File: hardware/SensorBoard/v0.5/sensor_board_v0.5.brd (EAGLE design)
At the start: 46.8 x 39.9 mm, 58 parts, among them J3 USB-MICROB, U1 ATMEGA328P, U2 TSL2561, U4 MPL115A, U5 FT231XS, U6 ADMP401, U7 SHT31-DIS, U8 MCP1703CB, U9 MCP1703CB, Y1 16MHZ

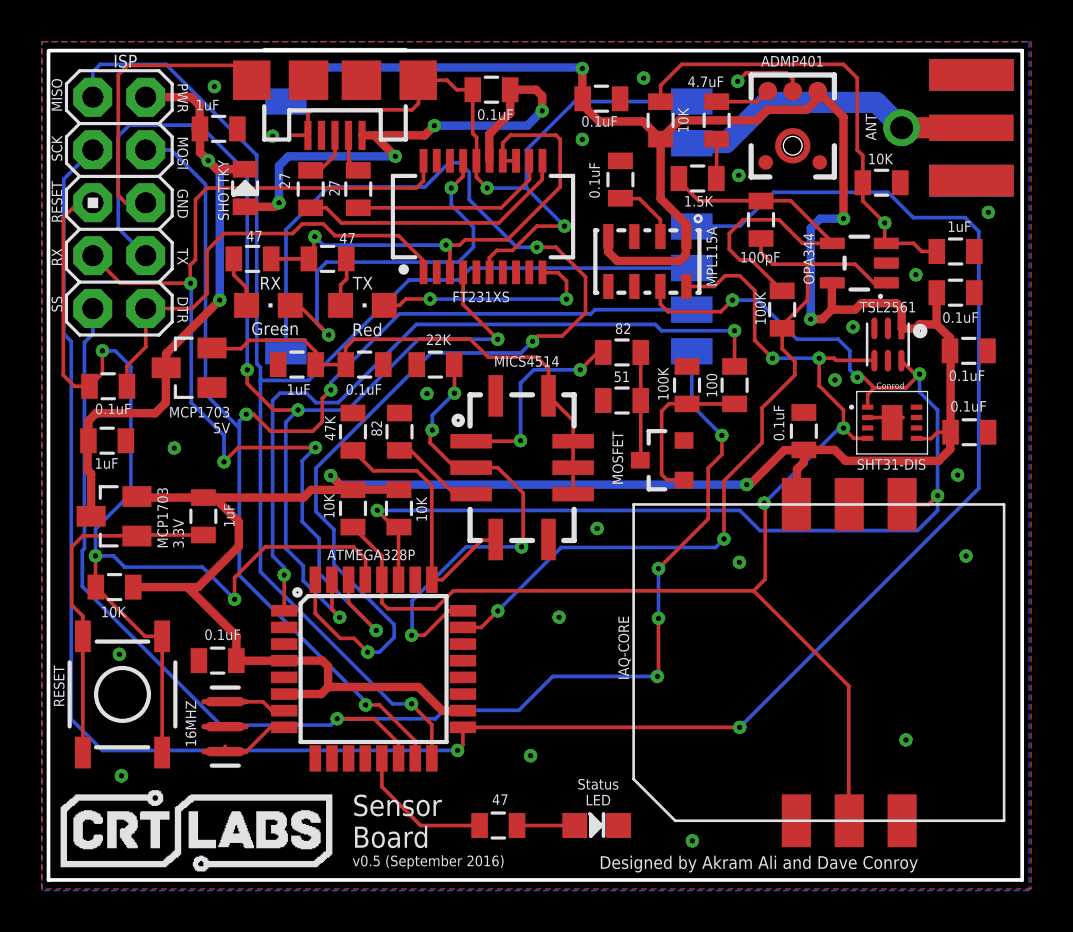
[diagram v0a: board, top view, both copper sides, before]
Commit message: Adjusted silk screen
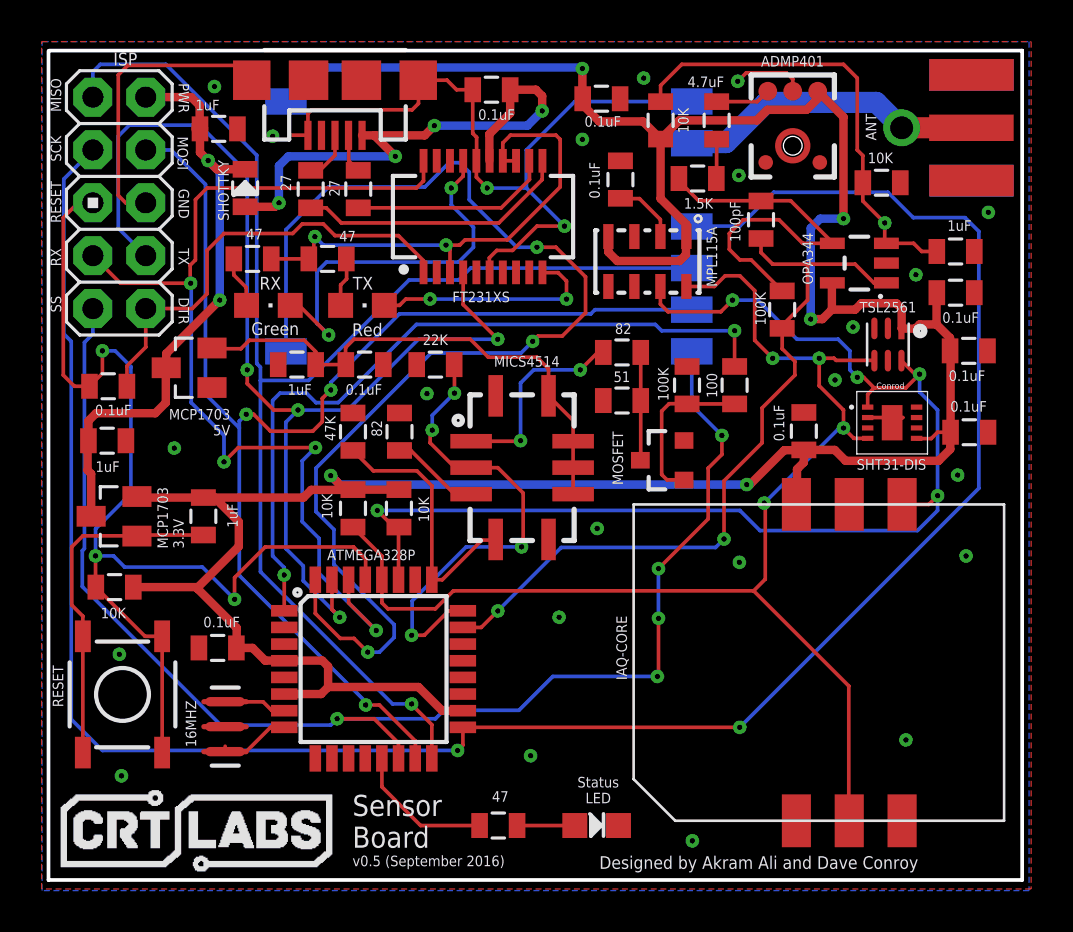
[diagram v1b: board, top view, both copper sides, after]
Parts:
- moved C15 0.61 mm to (14.0, 17.8)
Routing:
- net VCC: track 148.1 -> 147.6 mm

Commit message: Made the GND plane more consistent
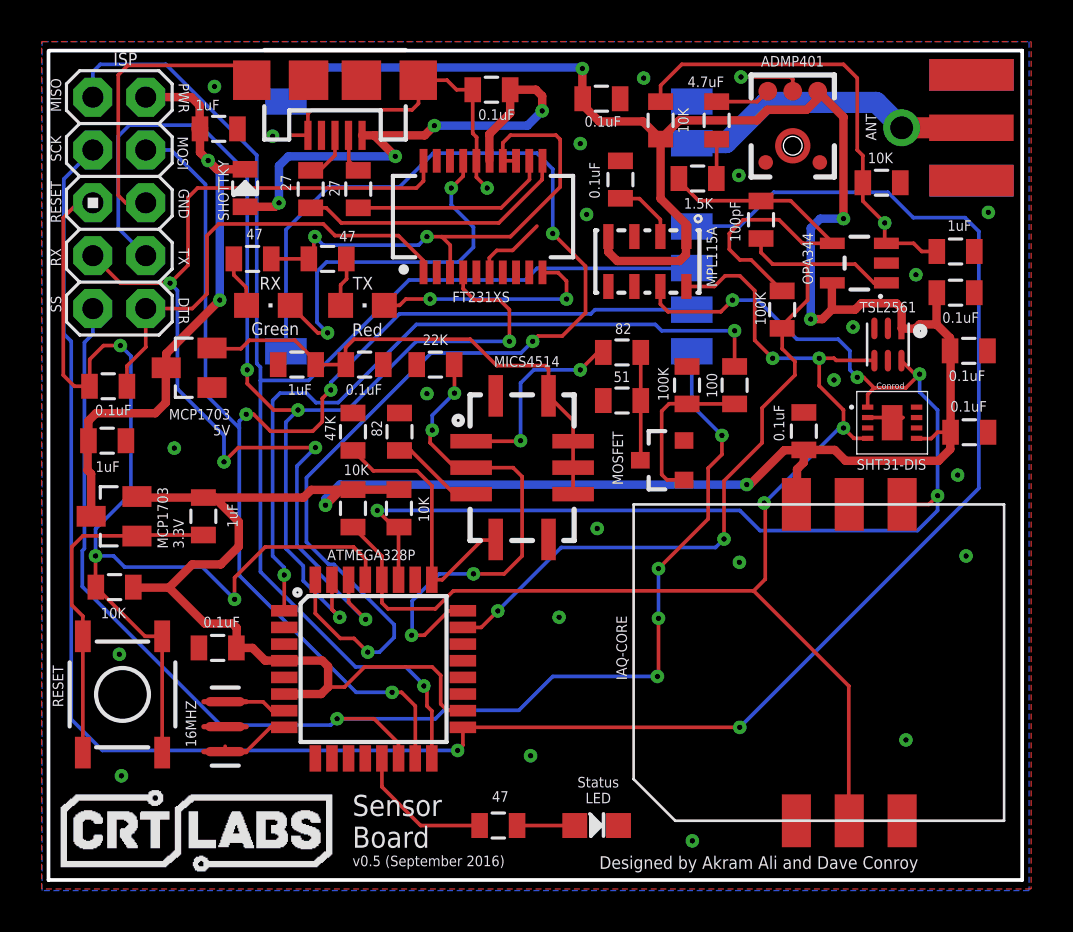
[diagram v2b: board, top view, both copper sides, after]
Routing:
- net GND: track 73.8 -> 56.8 mm
- net VCC: track 147.6 -> 151.5 mm
- net D2: track 58.6 -> 60.8 mm
- net TX: track 54.9 -> 56.5 mm
- net RX: track 49.3 -> 47.9 mm
- net MOSI: track 61.5 -> 62.4 mm
- net MISO: track 67.1 -> 67.9 mm
- net VNOX: track 23.3 -> 23.9 mm
- net RESET: track 52.5 -> 53.2 mm
- net FTDI_VCC: track 24.6 -> 25.1 mm

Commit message: Connected GND plane
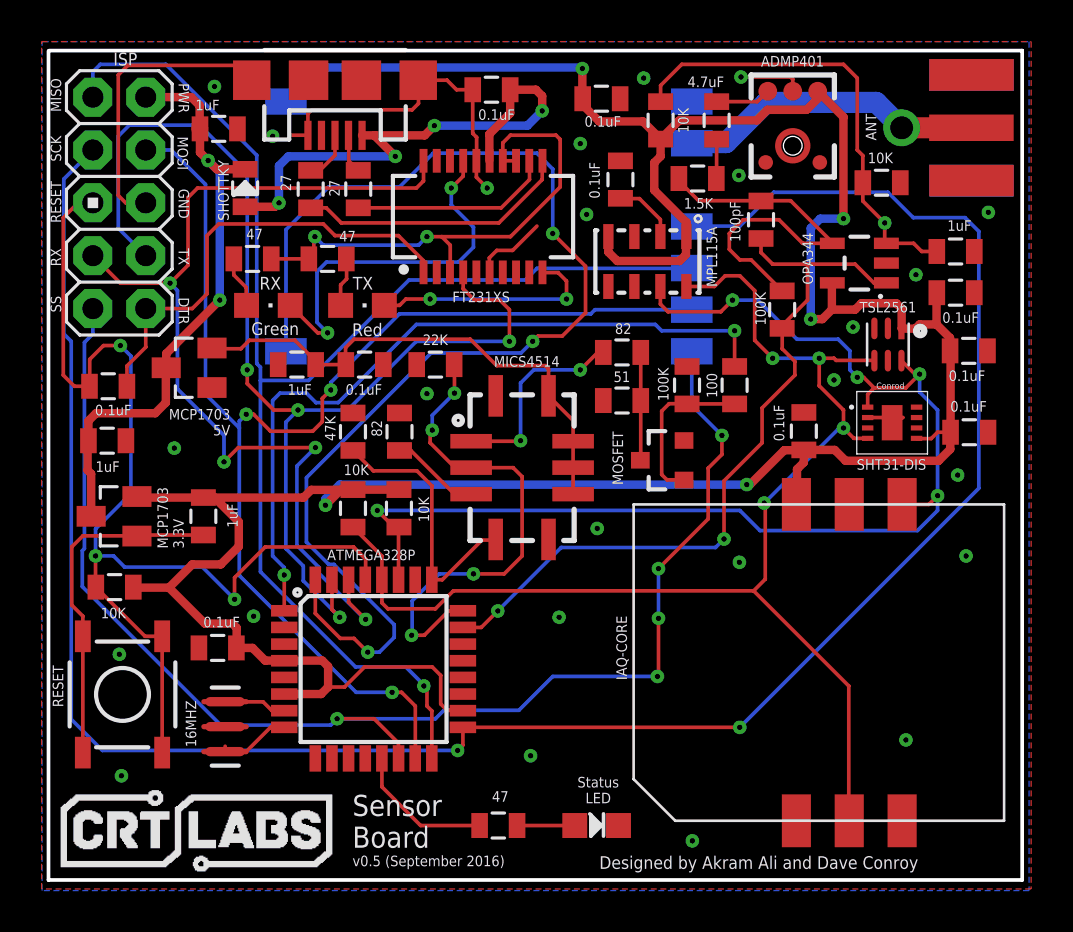
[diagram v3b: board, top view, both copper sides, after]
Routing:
- net GND: vias 24 -> 25
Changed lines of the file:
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@@
 <wire x1="41.5544" y1="45.212" x2="41.656" y2="45.1104" width="0.1778" layer="1"/>
 <wire x1="41.656" y1="45.1104" x2="41.656" y2="44.53" width="0.1778" layer="1"/>
-<wire x1="17.2212" y1="16.364" x2="17.2212" y2="17.964" width="0" layer="19" extent="1-1"/>
+<via x="15.748" y="19.304" extent="1-16" drill="0.254" diameter="0.127"/>
 </signal>
 <signal name="VCC">
@@
 <wire x1="42.9768" y1="38.4048" x2="42.5196" y2="37.9476" width="0.4064" layer="16"/>
 <wire x1="42.5196" y1="37.9476" x2="42.5196" y2="33.5788" width="0.4064" layer="16"/>
-<wire x1="36.546" y1="37.5474" x2="36.546" y2="38.13" width="0.4064" layer="1"/>
-<wire x1="36.546" y1="38.13" x2="35.306" y2="39.37" width="0.4064" layer="1"/>
-<wire x1="35.306" y1="39.37" x2="35.306" y2="42.2292" width="0.4064" layer="1"/>
 <contactref element="C15" pad="1"/>
 <wire x1="39.4462" y1="25.6286" x2="39.4462" y2="25.6794" width="0.4064" layer="1"/>
@@
 <wire x1="32.796" y1="37.5474" x2="32.796" y2="36.8" width="0.4064" layer="1"/>
 <wire x1="32.796" y1="36.8" x2="33.2232" y2="36.3728" width="0.4064" layer="1"/>
-<wire x1="33.2232" y1="36.3728" x2="36.2204" y2="36.3728" width="0.4064" layer="1"/>
-<wire x1="36.2204" y1="36.3728" x2="36.5252" y2="36.6776" width="0.4064" layer="1"/>
-<wire x1="36.5252" y1="36.6776" x2="36.5252" y2="37.5266" width="0.4064" layer="1"/>
-<wire x1="36.5252" y1="37.5266" x2="36.546" y2="37.5474" width="0.4064" layer="1"/>
 <wire x1="17.2148" y1="17.1704" x2="17.2212" y2="17.164" width="0.4064" layer="1"/>
 <wire x1="15.0368" y1="22.6568" x2="15.0368" y2="23.8362" width="0.4064" layer="1"/>
@@
 <wire x1="14.1732" y1="21.7932" x2="12.8016" y2="21.7932" width="0.4064" layer="1"/>
 <wire x1="12.8016" y1="21.7932" x2="11.684" y2="20.6756" width="0.4064" layer="1"/>
+<wire x1="35.306" y1="42.2292" x2="35.306" y2="41.402" width="0.4064" layer="1"/>
+<wire x1="35.306" y1="41.402" x2="35.0012" y2="41.0972" width="0.4064" layer="1"/>
+<wire x1="33.2232" y1="36.3728" x2="36.2204" y2="36.3728" width="0.4064" layer="1"/>
+<wire x1="36.2204" y1="36.3728" x2="36.5252" y2="36.6776" width="0.4064" layer="1"/>
+<wire x1="36.5252" y1="36.6776" x2="36.5252" y2="37.5266" width="0.4064" layer="1"/>
+<wire x1="36.5252" y1="37.5266" x2="36.546" y2="37.5474" width="0.4064" layer="1"/>
+<wire x1="36.546" y1="37.5474" x2="36.546" y2="38.2316" width="0.4064" layer="1"/>
+<wire x1="36.546" y1="38.2316" x2="35.0012" y2="39.7764" width="0.4064" layer="1"/>
+<wire x1="35.0012" y1="39.7764" x2="35.0012" y2="41.0972" width="0.4064" layer="1"/>
 </signal>
 <signal name="SCL">
@@
 <wire x1="27.432" y1="31.3436" x2="26.162" y2="32.6136" width="0.1778" layer="1"/>
 <wire x1="18.7308" y1="31.3944" x2="18.7308" y2="31.5612" width="0.1778" layer="1"/>
-<wire x1="18.7308" y1="31.5612" x2="17.7292" y2="32.5628" width="0.1778" layer="1"/>
 <wire x1="17.7292" y1="32.5628" x2="15.5448" y2="32.5628" width="0.1778" layer="1"/>
 <wire x1="15.5448" y1="32.5628" x2="15.1384" y2="32.1564" width="0.1778" layer="1"/>
+<wire x1="18.7308" y1="31.5612" x2="17.7292" y2="32.5628" width="0.1778" layer="1"/>
 </signal>
 <signal name="N$20">
